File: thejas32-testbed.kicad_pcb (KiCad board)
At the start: 4 copper layers, 141.5 x 110 mm, 132 parts, among them J1 Conn_02x04_Odd_Even, J10 Conn_02x10_Odd_Even, J11 Conn_02x03_Odd_Even, J13 Conn_02x06_Odd_Even, J15 Conn_01x04, J2 USB_B_Micro, J3 Conn_02x03_Odd_Even, J4 Conn_02x04_Odd_Even, J5 Conn_02x06_Odd_Even, J6 Conn_02x06_Odd_Even, J7 Conn_02x03_Odd_Even, J8 Conn_02x06_Odd_Even, J9 Conn_02x10_Odd_Even, U1 Pico Master, U2 THEJAS32, U3 Pico Slave, U4 MINI360 DC-DC, U5 MINI360 DC-DC, U6 W25Q16JVSSIQ

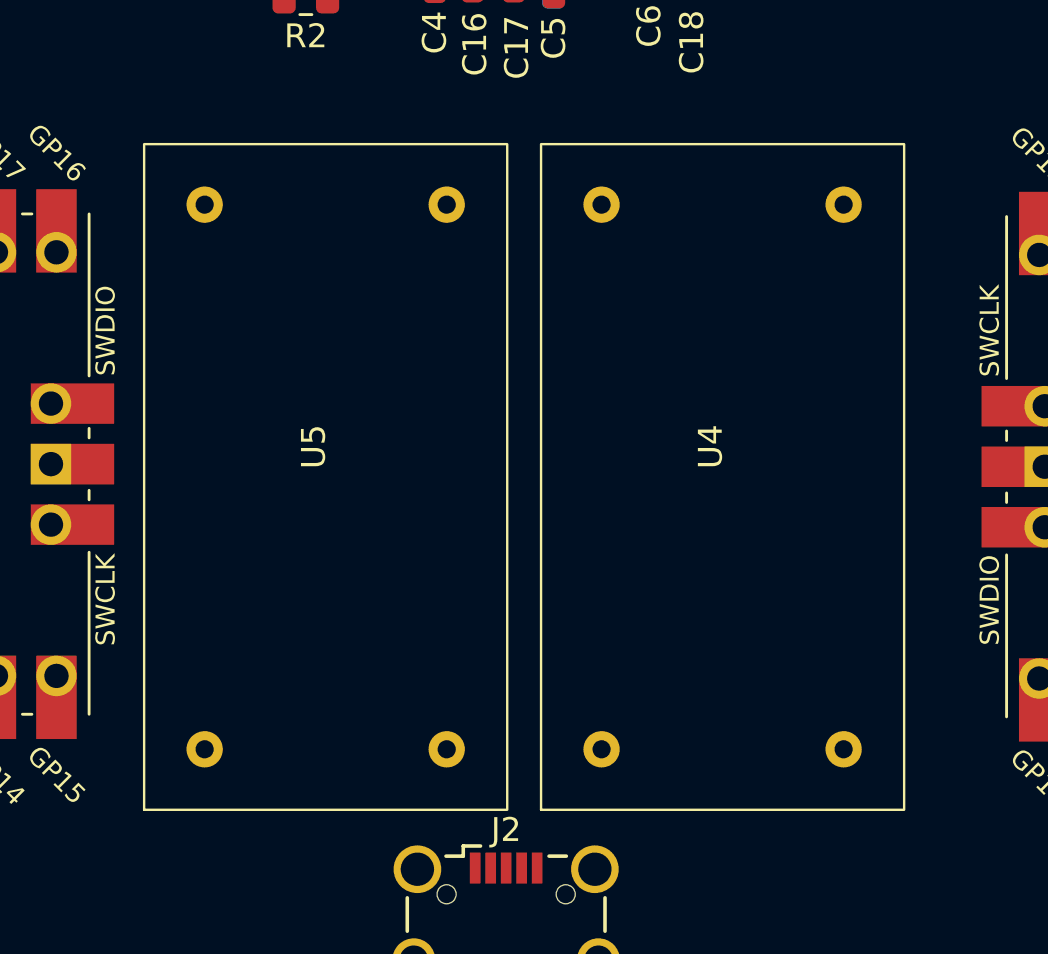
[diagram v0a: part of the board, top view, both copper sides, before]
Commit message: Add footprint for Mini360
Roughly tested using calipers against a physical module.

Source of footprint:

https://github.com/rayvburn/KiCad/tree/master/Mini360_step_down_converter/Mini360_step-down.pretty

Commit 69583e8
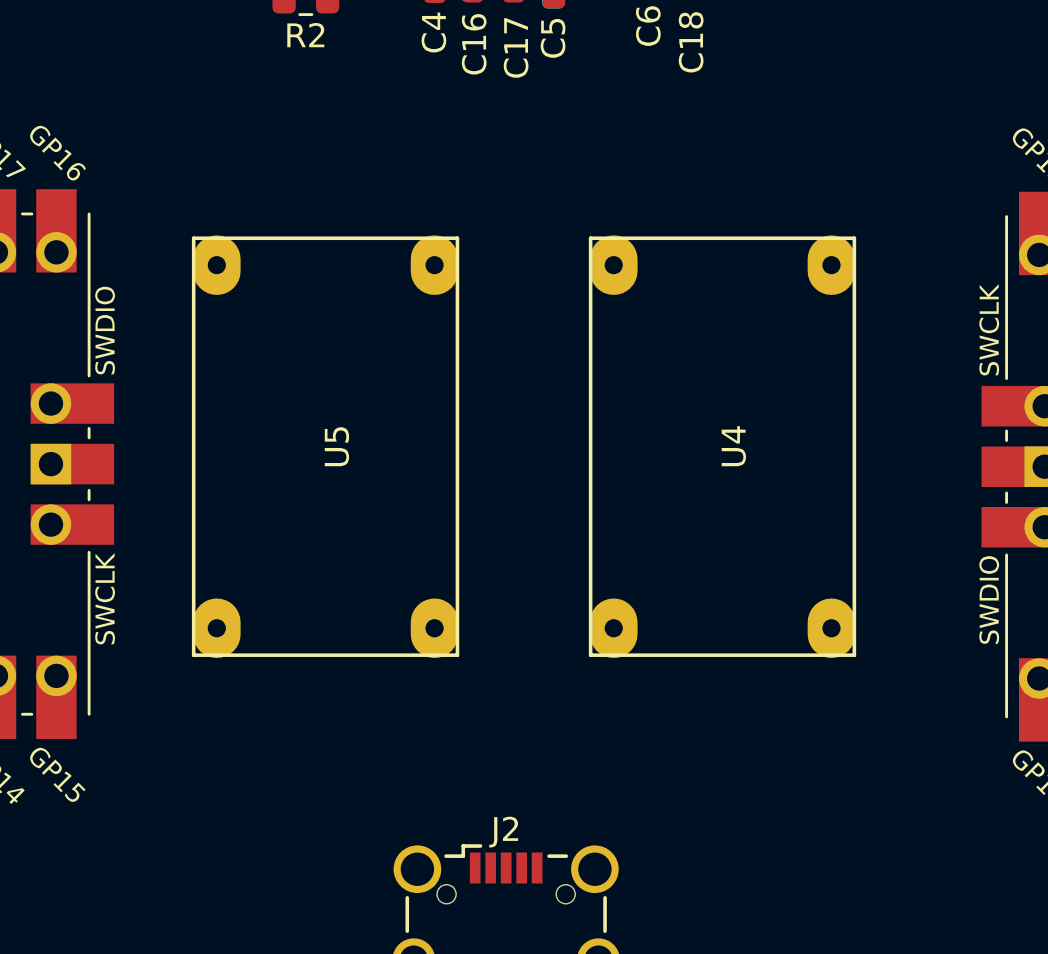
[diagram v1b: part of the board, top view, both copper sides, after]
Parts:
- U4, U5: footprint Module_DCDC:Mini 360 -> project_lib:Mini360_step-down
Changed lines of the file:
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@@
 		(sheetname "Root")
 		(sheetfile "thejas32-testbed.kicad_sch")
-		(attr exclude_from_pos_files exclude_from_bom)
+		(attr exclude_from_pos_files)
 		(fp_circle
 			(center 0 0)
@@
 		(sheetname "Root")
 		(sheetfile "thejas32-testbed.kicad_sch")
-		(attr exclude_from_pos_files exclude_from_bom)
+		(attr exclude_from_pos_files)
 		(fp_circle
 			(center 0 0)
@@
 		(sheetname "Root")
 		(sheetfile "thejas32-testbed.kicad_sch")
-		(attr exclude_from_pos_files exclude_from_bom)
+		(attr exclude_from_pos_files)
 		(fp_circle
 			(center 0 0)
@@
 		)
 	)
-	(footprint "Module_DCDC:Mini 360"
+	(footprint "project_lib:Mini360_step-down"
 		(layer "F.Cu")
 		(at 162.58 136.16 90)
 		(property "Reference" "U4"
-			(at 0 -0.5 90)
-			(unlocked yes)
+			(at 0 0.5 90)
 			(layer "F.SilkS")
 			(effects
 				(font
 					(size 1 1)
-					(thickness 0.1)
+					(thickness 0.15)
 				)
 			)
 		)
 		(property "Value" "MINI360 DC-DC"
-			(at 0 1 90)
-			(unlocked yes)
+			(at 0 -0.5 90)
 			(layer "F.Fab")
 			(effects
@@
 			)
 		)
-		(property "Footprint" "Module_DCDC:Mini 360"
+		(property "Footprint" "project_lib:Mini360_step-down"
 			(at 0 0 90)
 			(unlocked yes)
@@
 		(sheetfile "thejas32-testbed.kicad_sch")
 		(attr through_hole)
-		(fp_rect
-			(start -15.24 -7.62)
-			(end 12.7 7.62)
+		(fp_line
+			(start -8.75 -5.54)
+			(end 8.75 -5.54)
 			(stroke
-				(width 0.1)
-				(type default)
+				(width 0.15)
+				(type solid)
 			)
-			(fill none)
 			(layer "F.SilkS")
 		)
-		(fp_text user "${REFERENCE}"
-			(at 0 2.5 90)
-			(unlocked yes)
-			(layer "F.Fab")
-			(effects
-				(font
-					(size 1 1)
-					(thickness 0.15)
-				)
+		(fp_line
+			(start -8.75 -5.54)
+			(end -8.75 5.53)
+			(stroke
+				(width 0.15)
+				(type solid)
 			)
+			(layer "F.SilkS")
 		)
-		(pad "1" thru_hole circle
-			(at -12.7 -5.08 90)
-			(size 1.524 1.524)
+		(fp_line
+			(start 8.75 5.53)
+			(end 8.75 -5.54)
+			(stroke
+				(width 0.15)
+				(type solid)
+			)
+			(layer "F.SilkS")
+		)
+		(fp_line
+			(start 8.75 5.53)
+			(end -8.75 5.53)
+			(stroke
+				(width 0.15)
+				(type solid)
+			)
+			(layer "F.SilkS")
+		)
+		(pad "1" thru_hole oval
+			(at -7.62 -4.57 90)
+			(size 2.5 2)
 			(drill 0.762)
 			(layers "*.Cu" "*.Mask")
@@
 			(pintype "power_in")
 		)
-		(pad "2" thru_hole circle
-			(at -12.7 5.08 90)
-			(size 1.524 1.524)
+		(pad "2" thru_hole oval
+			(at -7.62 4.57 90)
+			(size 2.5 2)
 			(drill 0.762)
 			(layers "*.Cu" "*.Mask")
@@
 			(pintype "power_in")
 		)
-		(pad "3" thru_hole circle
-			(at 10.16 -5.08 90)
-			(size 1.524 1.524)
+		(pad "3" thru_hole oval
+			(at 7.62 -4.57 90)
+			(size 2.5 2)
 			(drill 0.762)
 			(layers "*.Cu" "*.Mask")
@@
 			(pintype "power_out")
 		)
-		(pad "4" thru_hole circle
-			(at 10.16 5.08 90)
-			(size 1.524 1.524)
+		(pad "4" thru_hole oval
+			(at 7.62 4.57 90)
+			(size 2.5 2)
 			(drill 0.762)
 			(layers "*.Cu" "*.Mask")
@@
 		)
 	)
-	(footprint "Module_DCDC:Mini 360"
+	(footprint "project_lib:Mini360_step-down"
 		(layer "F.Cu")
 		(at 145.92 136.16 90)
 		(property "Reference" "U5"
-			(at 0 -0.5 90)
-			(unlocked yes)
+			(at 0 0.5 90)
 			(layer "F.SilkS")
 			(effects
 				(font
 					(size 1 1)
-					(thickness 0.1)
+					(thickness 0.15)
 				)
 			)
 		)
 		(property "Value" "MINI360 DC-DC"
-			(at 0 1 90)
-			(unlocked yes)
+			(at 0 -0.5 90)
 			(layer "F.Fab")
 			(effects
@@
 			)
 		)
-		(property "Footprint" "Module_DCDC:Mini 360"
+		(property "Footprint" "project_lib:Mini360_step-down"
 			(at 0 0 90)
 			(unlocked yes)
@@
 		(sheetfile "thejas32-testbed.kicad_sch")
 		(attr through_hole)
-		(fp_rect
-			(start -15.24 -7.62)
-			(end 12.7 7.62)
+		(fp_line
+			(start -8.75 -5.54)
+			(end 8.75 -5.54)
 			(stroke
-				(width 0.1)
-				(type default)
+				(width 0.15)
+				(type solid)
 			)
-			(fill none)
 			(layer "F.SilkS")
 		)
-		(fp_text user "${REFERENCE}"
-			(at 0 2.5 90)
-			(unlocked yes)
-			(layer "F.Fab")
-			(effects
-				(font
-					(size 1 1)
-					(thickness 0.15)
-				)
+		(fp_line
+			(start -8.75 -5.54)
+			(end -8.75 5.53)
+			(stroke
+				(width 0.15)
+				(type solid)
 			)
+			(layer "F.SilkS")
 		)
-		(pad "1" thru_hole circle
-			(at -12.7 -5.08 90)
-			(size 1.524 1.524)
+		(fp_line
+			(start 8.75 5.53)
+			(end 8.75 -5.54)
+			(stroke
+				(width 0.15)
+				(type solid)
+			)
+			(layer "F.SilkS")
+		)
+		(fp_line
+			(start 8.75 5.53)
+			(end -8.75 5.53)
+			(stroke
+				(width 0.15)
+				(type solid)
+			)
+			(layer "F.SilkS")
+		)
+		(pad "1" thru_hole oval
+			(at -7.62 -4.57 90)
+			(size 2.5 2)
 			(drill 0.762)
 			(layers "*.Cu" "*.Mask")
@@
 			(pintype "power_in")
 		)
-		(pad "2" thru_hole circle
-			(at -12.7 5.08 90)
-			(size 1.524 1.524)
+		(pad "2" thru_hole oval
+			(at -7.62 4.57 90)
+			(size 2.5 2)
 			(drill 0.762)
 			(layers "*.Cu" "*.Mask")
@@
 			(pintype "power_in")
 		)
-		(pad "3" thru_hole circle
-			(at 10.16 -5.08 90)
-			(size 1.524 1.524)
+		(pad "3" thru_hole oval
+			(at 7.62 -4.57 90)
+			(size 2.5 2)
 			(drill 0.762)
 			(layers "*.Cu" "*.Mask")
@@
 			(pintype "power_out")
 		)
-		(pad "4" thru_hole circle
-			(at 10.16 5.08 90)
-			(size 1.524 1.524)
+		(pad "4" thru_hole oval
+			(at 7.62 4.57 90)
+			(size 2.5 2)
 			(drill 0.762)
 			(layers "*.Cu" "*.Mask")
@@
 		(sheetname "Root")
 		(sheetfile "thejas32-testbed.kicad_sch")
-		(attr exclude_from_pos_files exclude_from_bom)
+		(attr exclude_from_pos_files)
 		(fp_circle
 			(center 0 0)

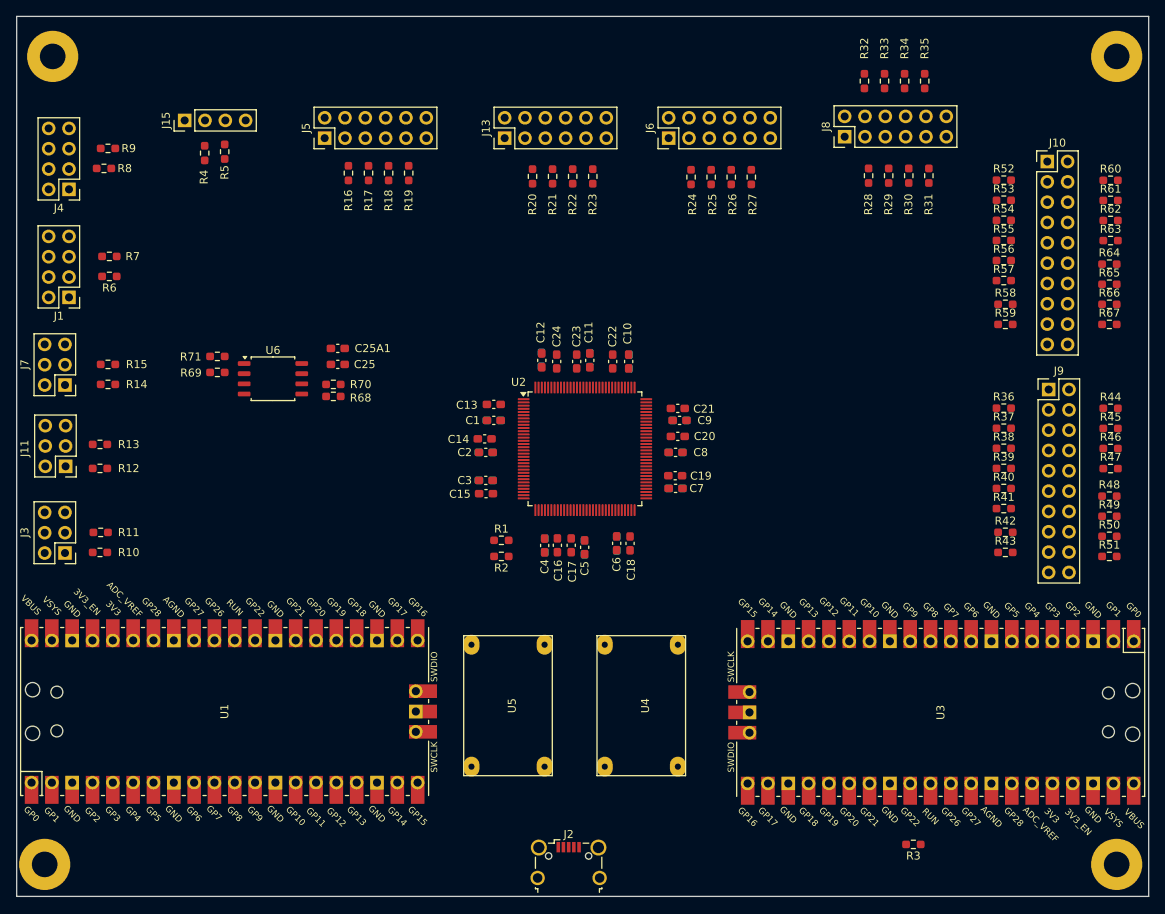
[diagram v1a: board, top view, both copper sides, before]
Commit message: Various simplifications, initial routing.
This is a commit for review.

Schematic is modified to remove many zero ohms. RPi
connector brought in.

Layout shows 3V3 and 1V2 power planes. Pin mapping
may need to change to avoid usage of layer 3 for
signals if possible.
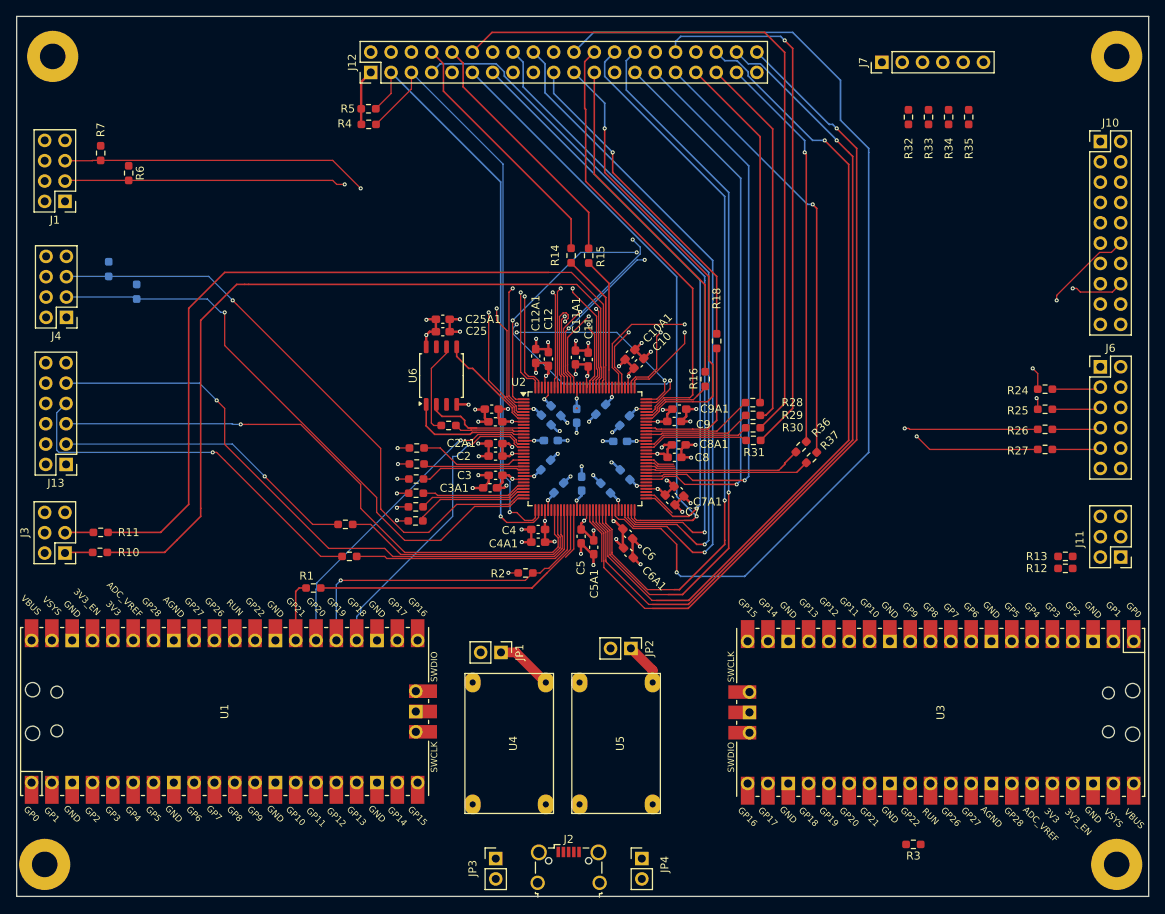
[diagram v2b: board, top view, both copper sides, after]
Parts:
- removed J15: Conn_01x04, Connector_PinHeader_2.54mm:PinHeader_1x04_P2.54mm_Vertical
- removed J5, J8: Conn_02x06_Odd_Even, Connector_PinHeader_2.54mm:PinHeader_2x06_P2.54mm_Vertical
- removed J9: Conn_02x10_Odd_Even, Connector_PinHeader_2.54mm:PinHeader_2x10_P2.54mm_Vertical
- removed R17, R19, R21, R23, R44, R45, R46, R47, R48, R49, R50, R51, R52, R53, R54, R55, R56, R57, R58, R59, R60, R61, R62, R63, R64, R65, R66, R67, R68, R69, R71: 0E, project_lib:proj_R_0603_1608Metric_Pad0.98x0.95mm_HandSolder
- added J12: Conn_02x20_Odd_Even, Connector_PinHeader_2.54mm:PinHeader_2x20_P2.54mm_Vertical, F.Cu at (128.8, 57.0)
- added JP1: Jumper_2_Bridged, Connector_PinHeader_2.54mm:PinHeader_1x02_P2.54mm_Vertical, F.Cu at (145.0, 129.5)
- added JP2: Jumper_2_Bridged, Connector_PinHeader_2.54mm:PinHeader_1x02_P2.54mm_Vertical, F.Cu at (161.3, 129.0)
- added JP3: Jumper_2_Bridged, Connector_PinHeader_2.54mm:PinHeader_1x02_P2.54mm_Vertical, F.Cu at (144.4, 155.3)
- added JP4: Jumper_2_Bridged, Connector_PinHeader_2.54mm:PinHeader_1x02_P2.54mm_Vertical, F.Cu at (162.6, 155.3)
- C10A1, C11A1, C12A1, C1A1, C2A1, C3A1, C4A1, C5A1, C6A1, C7A1, C8A1, C9A1: moved to F.Cu
- C13, C14, C15, C16, C17, C18, C19, C20, C21, C22, C23, C24, R8, R9: moved to B.Cu
- J7: value Conn_02x03_Odd_Even -> Conn_01x06; footprint Connector_PinHeader_2.54mm:PinHeader_2x03_P2.54mm_Vertical -> Connector_PinHeader_2.54mm:PinHeader_1x06_P2.54mm_Vertical
- R38, R39, R40, R41, R42, R43: value 0E -> 10K
- U4, U5: value MINI360 DC-DC -> ~
- moved J11 132.4 mm to (222.5, 117.6)
- moved R13 121.5 mm to (215.6, 117.5), turned to 0 degrees
- moved R12 121.3 mm to (215.6, 119.0), turned to 0 degrees
- moved J7 109.8 mm to (192.7, 55.7), turned to 90 degrees
- moved R43 73.8 mm to (134.4, 113.1)
- moved R42 73.8 mm to (134.4, 111.3)
- moved R41 73.5 mm to (134.4, 109.6)
- moved R40 73.5 mm to (134.4, 107.8)
- moved R39 73.4 mm to (134.5, 105.9)
- moved R38 73.4 mm to (134.5, 103.9)
- moved J13 68.3 mm to (90.7, 106.0), turned to 180 degrees
- moved R15 61.6 mm to (156.0, 79.9), turned to 90 degrees
- moved J6 61.1 mm to (220.0, 93.8), turned to 0 degrees
- moved R14 60.1 mm to (153.8, 79.9), turned to 90 degrees
- moved R22 55.1 mm to (126.1, 117.5), turned to 180 degrees
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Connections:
- net Net-(J15-Pin_2) renamed RPi_COMPAT_I2C1_SCL
- net Net-(J15-Pin_3) renamed RPi_COMPAT_I2C1_SDA
- net Net-(J2-VBUS) renamed PWR_5V
- C25 pad 1: +3V3 -> PWR_3V3
- C25A1 pad 1: +3V3 -> PWR_3V3
- J10 pad 1: +3V3 -> PWR_3V3
- J10 pad 2: +3V3 -> PWR_3V3
- J13 pad 1: +3V3 -> PWR_3V3
- J13 pad 2: +3V3 -> PWR_3V3
- J6 pad 1: +3V3 -> PWR_3V3
- J6 pad 2: +3V3 -> PWR_3V3
- J7 pad 1: Net-(J7-Pin_1) -> PWR_3V3
- J7 pad 2: MCU_UART2_TX -> MCU_PWM_4
- J7 pad 3: Net-(J7-Pin_3) -> MCU_PWM_5
- J7 pad 4: MCU_UART2_RX -> MCU_PWM_6
- J7 pad 5: GND -> MCU_PWM_7
- R14 pad 2: Net-(J7-Pin_1) -> RPi_COMPAT_UART_TXD
- R15 pad 2: Net-(J7-Pin_3) -> RPi_COMPAT_UART_RXD
- R16 pad 2: Net-(J5-Pin_3) -> RPi_COMPAT_SPI0_SCLK
- R18 pad 2: Net-(J5-Pin_7) -> RPi_COMPAT_SPI0_MOSI
- R28 pad 2: MCU_PWM_0 -> RPi_COMPAT_PWM1
- R29 pad 2: MCU_PWM_1 -> RPi_COMPAT_PWM1_ALT
- R30 pad 2: MCU_PWM_2 -> RPi_COMPAT_PWM0
- R31 pad 2: MCU_PWM_3 -> RPi_COMPAT_PWM0_ALT
- R36 pad 2: MCU_GPIO_00 -> RPi_COMPAT_GPIO_26
- R37 pad 2: MCU_GPIO_01 -> RPi_COMPAT_GPIO_6
- R38 pad 1: Net-(U2-GPIO2) -> GND
- R38 pad 2: MCU_GPIO_02 -> MCU_TST_CLK
- R39 pad 1: Net-(U2-GPIO3) -> GND
- R39 pad 2: MCU_GPIO_03 -> MCU_TJTAG_TMS
- R40 pad 1: Net-(U2-GPIO4) -> GND
- R40 pad 2: MCU_GPIO_04 -> MCU_TJTAG_TDI
- R41 pad 1: Net-(U2-GPIO5) -> GND
- R41 pad 2: MCU_GPIO_05 -> MCU_TJTAG_TCK
- R42 pad 1: Net-(U2-GPIO6) -> GND
- R42 pad 2: MCU_GPIO_06 -> MCU_TJTAG_TRST
- R43 pad 1: Net-(U2-GPIO7) -> GND
- R43 pad 2: MCU_GPIO_07 -> MCU_TST_MODE
- U1 pad 4: MCU_GPIO_00 -> unconnected-(U1-GPIO2-Pad4)_0
- U1 pad 40: unconnected-(U1-VBUS-Pad40) -> Net-(JP3-B)
- U1 pad 5: MCU_GPIO_01 -> unconnected-(U1-GPIO3-Pad5)
- U2 pad 1: Net-(U2-GPIO19) -> MCU_GPIO_19
- U2 pad 109: Net-(U2-GPIO31) -> MCU_GPIO_31
- U2 pad 110: Net-(U2-GPIO30) -> MCU_GPIO_30
- U2 pad 111: Net-(U2-GPIO29) -> MCU_GPIO_29
- U2 pad 116: Net-(U2-GPIO28) -> MCU_GPIO_28
- U2 pad 117: Net-(U2-GPIO27) -> MCU_GPIO_27
- U2 pad 118: Net-(U2-GPIO26) -> MCU_GPIO_26
- U2 pad 119: Net-(U2-GPIO25) -> MCU_GPIO_25
- U2 pad 120: Net-(U2-GPIO24) -> MCU_GPIO_24
- U2 pad 121: Net-(U2-GPIO23) -> MCU_GPIO_23
- U2 pad 122: Net-(U2-GPIO22) -> MCU_GPIO_22
- U2 pad 127: Net-(U2-GPIO21) -> MCU_GPIO_21
- U2 pad 128: Net-(U2-GPIO20) -> MCU_GPIO_20
- U2 pad 2: Net-(U2-GPIO18) -> MCU_GPIO_18
- U2 pad 20: unconnected-(U2-TST_CLK-Pad20) -> MCU_TST_CLK
- U2 pad 22: unconnected-(U2-TJTAG_TMS-Pad22) -> MCU_TJTAG_TMS
- U2 pad 23: unconnected-(U2-TJTAG_TDI-Pad23) -> MCU_TJTAG_TDI
- U2 pad 28: unconnected-(U2-TJTAG_TCK-Pad28) -> MCU_TJTAG_TCK
- U2 pad 29: unconnected-(U2-TJTAG_TRST-Pad29) -> MCU_TJTAG_TRST
- U2 pad 30: unconnected-(U2-TST_MODE-Pad30) -> MCU_TST_MODE
- U2 pad 39: Net-(U2-SPI1_SS) -> Net-(J13-Pin_5)
- U2 pad 41: Net-(U2-SPI1_MISO) -> Net-(J13-Pin_9)
- U2 pad 5: Net-(U2-GPIO17) -> MCU_GPIO_17
- U2 pad 51: Net-(U2-GPIO15) -> RPi_COMPAT_GPIO_21
- U2 pad 52: Net-(U2-GPIO14) -> RPi_COMPAT_GPIO_20
- U2 pad 53: Net-(U2-GPIO13) -> RPi_COMPAT_GPIO_16
- U2 pad 54: Net-(U2-GPIO12) -> RPi_COMPAT_GPIO_1
- U2 pad 55: Net-(U2-GPIO11) -> RPi_COMPAT_GPIO_7
- U2 pad 58: Net-(U2-GPIO10) -> RPi_COMPAT_GPIO_25
- U2 pad 6: Net-(U2-GPIO16) -> MCU_GPIO_16
- U2 pad 61: Net-(U2-GPIO9) -> RPi_COMPAT_GPIO_24
- U2 pad 62: Net-(U2-GPIO8) -> RPi_COMPAT_GPIO_23
- U2 pad 63: Net-(U2-GPIO7) -> RPi_COMPAT_GPIO_4
- U2 pad 64: Net-(U2-GPIO6) -> RPi_COMPAT_GPIO_17
- U2 pad 65: Net-(U2-GPIO5) -> RPi_COMPAT_GPIO_27
- U2 pad 66: Net-(U2-GPIO4) -> RPi_COMPAT_GPIO_22
- U2 pad 71: Net-(U2-GPIO3) -> RPi_COMPAT_GPIO_0
- U2 pad 72: Net-(U2-GPIO2) -> RPi_COMPAT_GPIO_5
- U2 pad 90: Net-(U2-SPI0_MISO) -> RPi_COMPAT_SPI0_MISO
- U2 pad 92: Net-(U2-SPI0_CSN) -> RPi_COMPAT_SPI0_CE0
- U3 pad 40: unconnected-(U3-VBUS-Pad40) -> Net-(JP4-B)
- U3 pad 6: unconnected-(U3-GPIO4-Pad6) -> MCU_UART1_RX
- U3 pad 7: unconnected-(U3-GPIO5-Pad7) -> MCU_UART1_TX
- U4 pad 4: PWR_3V3 -> Net-(JP1-A)
- U5 pad 4: PWR_1V2 -> Net-(JP2-A)
- U6 pad 1: Net-(U6-~{CS}) -> Net-(U2-SPI3_SS)
- U6 pad 2: Net-(U6-DO(IO1)) -> Net-(U2-SPI3_MISO)
- U6 pad 5: Net-(U6-DI(IO0)) -> Net-(U2-SPI3_MOSI)
- U6 pad 8: +3V3 -> PWR_3V3
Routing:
- net RPi_COMPAT_GPIO_25: track 0.00 -> 128.8 mm, vias 0 -> 1
- net MCU_GPIO_24: track 0.00 -> 109.6 mm, vias 0 -> 1
- net RPi_COMPAT_GPIO_21: track 0.00 -> 104.1 mm, vias 0 -> 1
- net RPi_COMPAT_GPIO_16: track 0.00 -> 104.0 mm, vias 0 -> 1
- net RPi_COMPAT_GPIO_20: track 0.00 -> 103.9 mm, vias 0 -> 1
- net Net-(U2-UART0_RX): track 0.00 -> 101.9 mm
- net Net-(U2-UART0_TX): track 0.00 -> 101.2 mm
- net MCU_GPIO_16: track 0.00 -> 100.5 mm, vias 0 -> 1
- net MCU_GPIO_25: track 0.00 -> 100.0 mm, vias 0 -> 1
- net MCU_GPIO_17: track 0.00 -> 97.9 mm, vias 0 -> 1
- net MCU_GPIO_18: track 0.00 -> 94.4 mm, vias 0 -> 1
- net Net-(J1-Pin_5): track 0.00 -> 93.7 mm, vias 0 -> 3
- net RPi_COMPAT_GPIO_1: track 0.00 -> 93.1 mm, vias 0 -> 1
- net MCU_GPIO_19: track 0.00 -> 92.7 mm, vias 0 -> 2
- net MCU_GPIO_21: track 0.00 -> 92.7 mm, vias 0 -> 1
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- added copper zone on In2.Cu, net PWR_1V2
- added copper zone on In2.Cu, net PWR_3V3
